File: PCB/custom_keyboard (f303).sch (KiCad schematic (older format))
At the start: 363 parts, among them J1 Conn_01x04, J2 SM04B-SRSS-TB(LF)(SN), SW1 SW_Push, SW2 SW_Push, U1 SRV05-4, U12 XC6206P332MR, U13 74LVC1G34, U14 STM32F303CBT6, X1 TestPoint_Small, X2 TestPoint_Small, Y2 8MHz

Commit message: Added indicator LED
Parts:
- added D1: Green, LED_SMD:LED_0805_2012Metric, symbol Device:LED_Small
- added R2: 680, Resistor_SMD:R_0805_2012Metric, symbol Device:R_Small
- R64: value 510 -> 680; LCSC Part C17734 -> C17798
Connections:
- net +3V3: now also J1.1 (Pin_1)
- net +5V: no longer D2.2 (A), F1.2, FB15.2, J2.1 (Pin_1), U1.5 (VP), USB1.11 (VBUS), USB1.2 (VBUS)
- net GND: now also R2.1
- net KEYBOARD_RESET: no longer J1.1 (Pin_1)
- net ROW3: now also D1.2 (A)
- new net: D1.1 (K), R2.2
- new net VBUS: D2.2 (A), F1.2, FB15.2, J2.1 (Pin_1), U1.5 (VP), USB1.11 (VBUS), USB1.2 (VBUS)
- no-connect marks 4 -> 6
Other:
- moved on the sheet: C1, D11, F1, J1, R64

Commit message: Removed encoder resistors and capacitors
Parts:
- removed C10, C11, C8, C9: 100nF, Capacitor_SMD:C_0805_2012Metric, symbol Device:C_Small
- removed R15, R16, R17, R18: 10k, Resistor_SMD:R_0805_2012Metric, symbol Device:R_Small
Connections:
- net ENCODER_A: now also ROT1.A, ROT2.A
- net ENCODER_B1: now also ROT1.B
- net ENCODER_B2: now also ROT2.B
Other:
- note added: "Keyboard Crystal"
- note removed: "Keyboard Crystals"
- moved on the sheet: BKL3, BOOT0, BOOT1, C18, C19, C20, C21, C22, C23, C24, C43, C44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

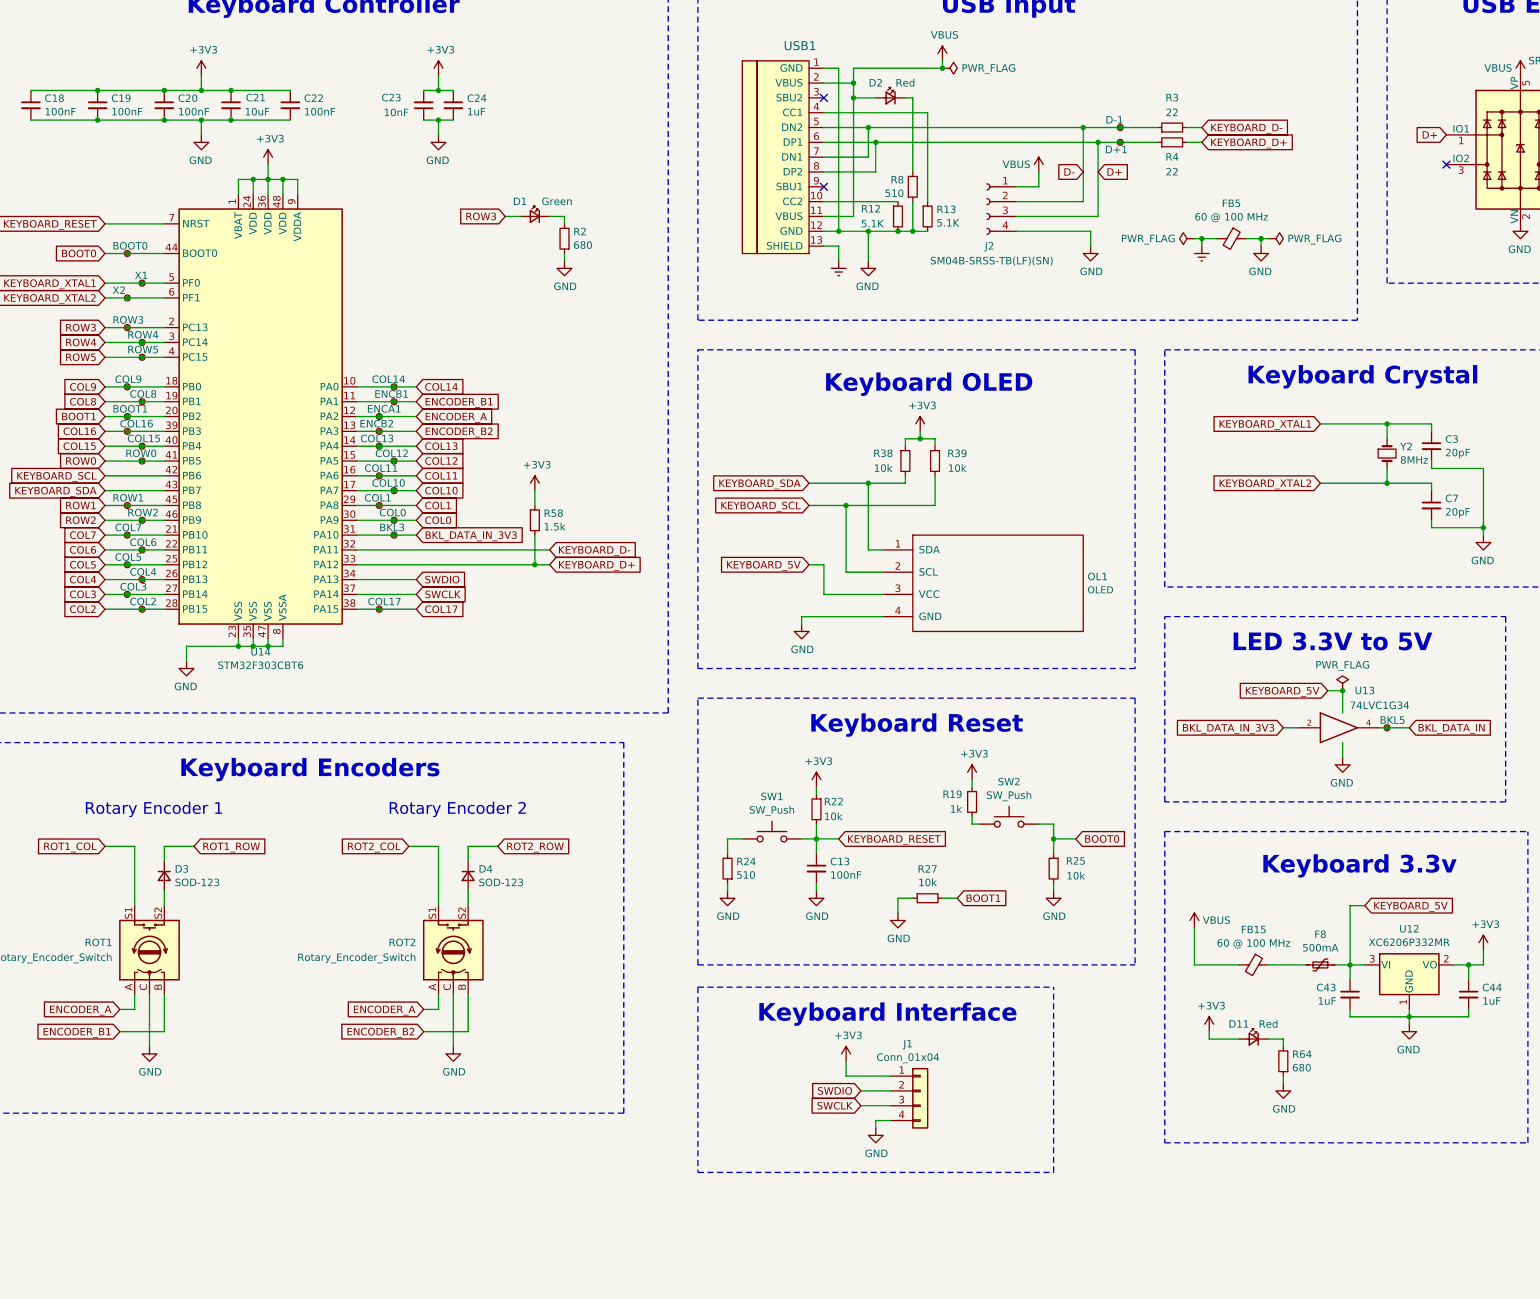
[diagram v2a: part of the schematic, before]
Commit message: Daisy chain routed diodes
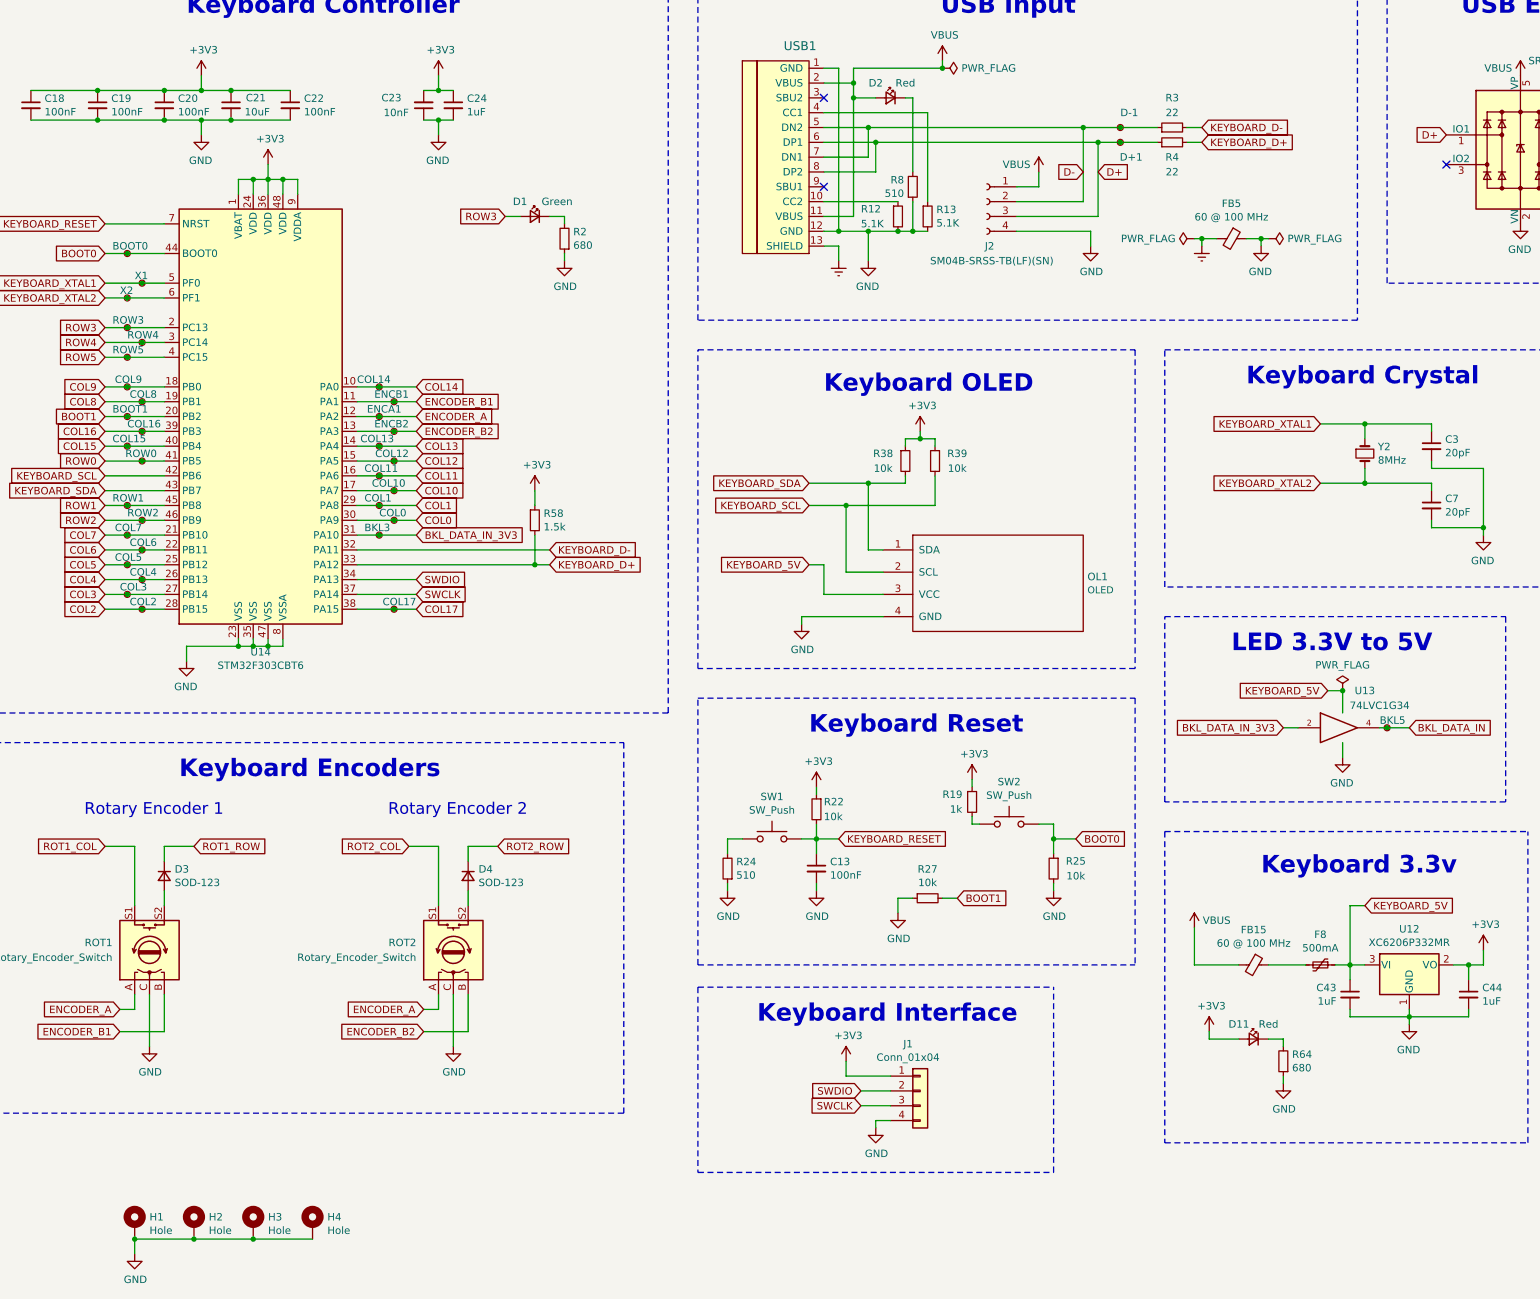
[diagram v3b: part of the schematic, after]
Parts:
- added H1, H2, H3, H4: Hole, MountingHole:MountingHole_3.2mm_M3_Pad, symbol Mechanical:MountingHole_Pad
- FB15, FB5: LCSC Part C237300 -> C337883
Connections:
- net GND: now also H1.1, H2.1, H3.1, H4.1
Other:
- moved on the sheet: BKL3, COL14, COL15, COL16, COL17, ENCB2, ROW5, Y2

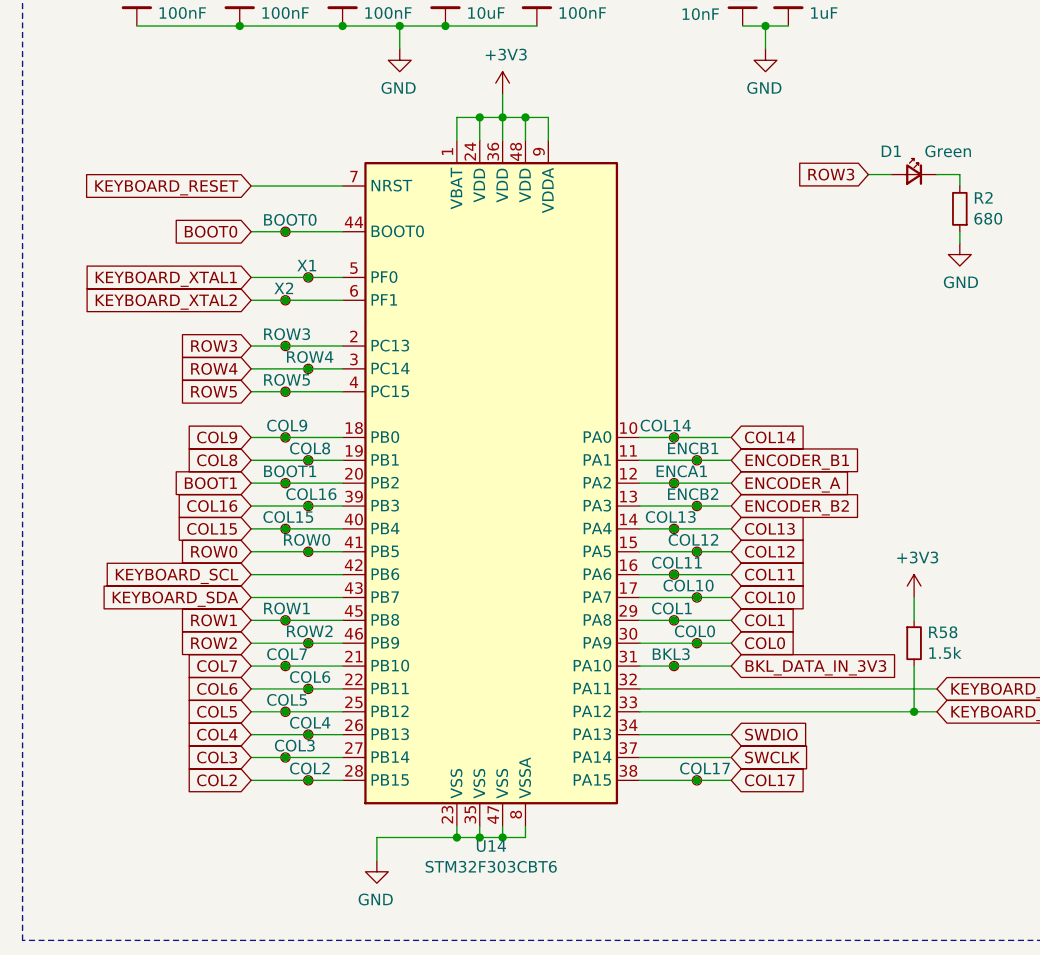
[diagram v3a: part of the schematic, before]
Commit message: Reassigned PC13/14/15
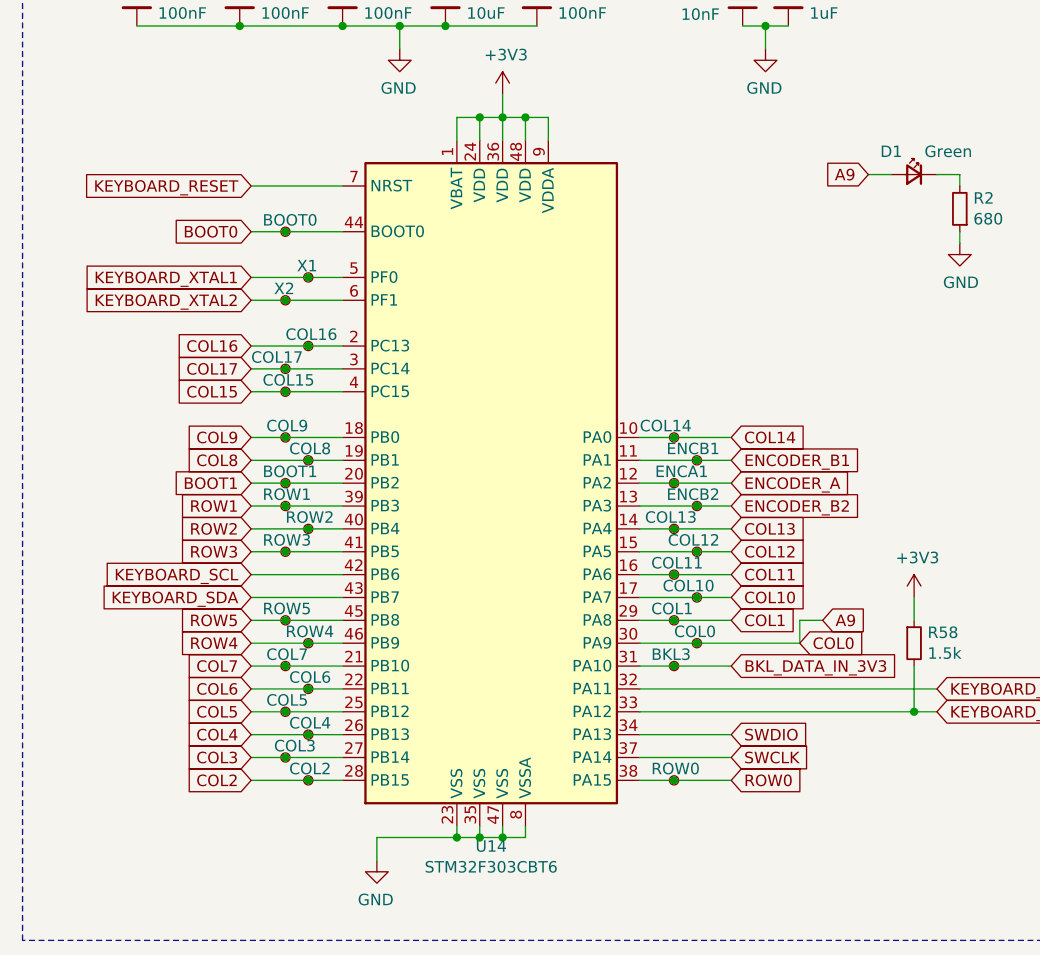
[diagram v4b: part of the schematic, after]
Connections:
- net COL15: now also U14.4 (PC15); no longer U14.40 (PB4)
- net COL16: now also U14.2 (PC13); no longer U14.39 (PB3)
- net COL17: now also U14.3 (PC14); no longer U14.38 (PA15)
- net ROT1_ROW: now also U14.38 (PA15); no longer U14.41 (PB5)
- net ROW1: now also U14.39 (PB3); no longer U14.45 (PB8)
- net ROW2: now also U14.40 (PB4); no longer U14.46 (PB9)
- net ROW3: now also U14.41 (PB5); no longer D1.2 (A), U14.2 (PC13)
- net ROW4: now also U14.46 (PB9); no longer U14.3 (PC14)
- net ROW5: now also U14.45 (PB8); no longer U14.4 (PC15)
- net COL0 renamed A9
- net A9: now also D1.2 (A)
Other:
- moved on the sheet: COL15, COL16, COL17, ROW0, ROW1, ROW2, ROW3, ROW4, ROW5

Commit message: Moved traces over by 1 gridline
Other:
- note added: "Mounting holes"
- moved on the sheet: D1, H1, H2, H3, H4, R2
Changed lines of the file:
@@
 Wire Notes Line
 	20050 11850 21850 11850
-Text Notes 17950 12150 2    118  ~ 24
+Text Notes 18100 12150 2    118  ~ 24
 USB Input
 Text GLabel 18000 13200 0    50   Input ~ 0
@@
 $EndComp
 Wire Wire Line
-	14500 13500 14500 13550
-Wire Wire Line
-	14400 13500 14500 13500
+	14300 13550 14300 13600
+Wire Wire Line
+	14200 13550 14300 13550
 $Comp
 L Device:R_Small R2
 U 1 1 75512E23
-P 14500 13650
-F 0 "R2" H 14441 13604 50  0000 R CNN
-F 1 "680" H 14441 13695 50  0000 R CNN
-F 2 "Resistor_SMD:R_0805_2012Metric" H 14500 13650 50  0001 C CNN
-F 3 "~" H 14500 13650 50  0001 C CNN
-F 4 "C17798" H 14500 13650 50  0001 C CNN "LCSC Part"
-	1    14500 13650
+P 14300 13700
+F 0 "R2" H 14241 13654 50  0000 R CNN
+F 1 "680" H 14241 13745 50  0000 R CNN
+F 2 "Resistor_SMD:R_0805_2012Metric" H 14300 13700 50  0001 C CNN
+F 3 "~" H 14300 13700 50  0001 C CNN
+F 4 "C17798" H 14300 13700 50  0001 C CNN "LCSC Part"
+	1    14300 13700
 	-1   0    0    1
 $EndComp
 Wire Wire Line
-	14500 13750 14500 13800
+	14300 13800 14300 13850
 $Comp
 L Device:LED_Small D1
 U 1 1 75512E2F
-P 14300 13500
-F 0 "D1" H 14400 13600 50  0000 C CNN
-F 1 "Green" H 14150 13600 50  0000 C CNN
-F 2 "LED_SMD:LED_0805_2012Metric" V 14300 13500 50  0001 C CNN
-F 3 "~" V 14300 13500 50  0001 C CNN
-F 4 "C84256" H 14300 13500 50  0001 C CNN "LCSC Part"
-	1    14300 13500
+P 14100 13550
+F 0 "D1" H 14200 13650 50  0000 C CNN
+F 1 "Green" H 13950 13650 50  0000 C CNN
+F 2 "LED_SMD:LED_0805_2012Metric" V 14100 13550 50  0001 C CNN
+F 3 "~" V 14100 13550 50  0001 C CNN
+F 4 "C84256" H 14100 13550 50  0001 C CNN "LCSC Part"
+	1    14100 13550
 	-1   0    0    -1
 $EndComp
@@
 L power:GND #PWR0194
 U 1 1 75512E39
-P 14500 13800
-F 0 "#PWR0194" H 14500 13550 50  0001 C CNN
-F 1 "GND" H 14505 13627 50  0000 C CNN
-F 2 "" H 14500 13800 50  0001 C CNN
-F 3 "" H 14500 13800 50  0001 C CNN
-	1    14500 13800
-	1    0    0    -1
-$EndComp
-Wire Wire Line
-	14200 13500 14100 13500
+P 14300 13850
+F 0 "#PWR0194" H 14300 13600 50  0001 C CNN
+F 1 "GND" H 14305 13677 50  0000 C CNN
+F 2 "" H 14300 13850 50  0001 C CNN
+F 3 "" H 14300 13850 50  0001 C CNN
+	1    14300 13850
+	1    0    0    -1
+$EndComp
+Wire Wire Line
+	14000 13550 13900 13550
 Text GLabel 13450 17750 0    50   Input ~ 0
 ROT2_COL
@@
 L Mechanical:MountingHole_Pad H1
 U 1 1 6C24E77E
-P 11600 20300
-F 0 "H1" H 11700 20349 50  0000 L CNN
-F 1 "Hole" H 11700 20258 50  0000 L CNN
-F 2 "MountingHole:MountingHole_3.2mm_M3_Pad" H 11600 20300 50  0001 C CNN
-F 3 "~" H 11600 20300 50  0001 C CNN
-	1    11600 20300
+P 21450 19250
+F 0 "H1" H 21550 19299 50  0000 L CNN
+F 1 "Hole" H 21550 19208 50  0000 L CNN
+F 2 "MountingHole:MountingHole_3.2mm_M3_Pad" H 21450 19250 50  0001 C CNN
+F 3 "~" H 21450 19250 50  0001 C CNN
+	1    21450 19250
 	1    0    0    -1
 $EndComp
@@
 L power:GND #PWR0199
 U 1 1 6C24F04A
-P 11600 20500
-F 0 "#PWR0199" H 11600 20250 50  0001 C CNN
-F 1 "GND" H 11605 20327 50  0000 C CNN
-F 2 "" H 11600 20500 50  0001 C CNN
-F 3 "" H 11600 20500 50  0001 C CNN
-	1    11600 20500
+P 21450 19450
+F 0 "#PWR0199" H 21450 19200 50  0001 C CNN
+F 1 "GND" H 21455 19277 50  0000 C CNN
+F 2 "" H 21450 19450 50  0001 C CNN
+F 3 "" H 21450 19450 50  0001 C CNN
+	1    21450 19450
 	1    0    0    -1
 $EndComp
@@
 L Mechanical:MountingHole_Pad H2
 U 1 1 6C24F523
-P 12000 20300
-F 0 "H2" H 12100 20349 50  0000 L CNN
-F 1 "Hole" H 12100 20258 50  0000 L CNN
-F 2 "MountingHole:MountingHole_3.2mm_M3_Pad" H 12000 20300 50  0001 C CNN
-F 3 "~" H 12000 20300 50  0001 C CNN
-	1    12000 20300
+P 21850 19250
+F 0 "H2" H 21950 19299 50  0000 L CNN
+F 1 "Hole" H 21950 19208 50  0000 L CNN
+F 2 "MountingHole:MountingHole_3.2mm_M3_Pad" H 21850 19250 50  0001 C CNN
+F 3 "~" H 21850 19250 50  0001 C CNN
+	1    21850 19250
 	1    0    0    -1
 $EndComp
@@
 L Mechanical:MountingHole_Pad H3
 U 1 1 6C24F72A
-P 12400 20300
-F 0 "H3" H 12500 20349 50  0000 L CNN
-F 1 "Hole" H 12500 20258 50  0000 L CNN
-F 2 "MountingHole:MountingHole_3.2mm_M3_Pad" H 12400 20300 50  0001 C CNN
-F 3 "~" H 12400 20300 50  0001 C CNN
-	1    12400 20300
+P 22250 19250
+F 0 "H3" H 22350 19299 50  0000 L CNN
+F 1 "Hole" H 22350 19208 50  0000 L CNN
+F 2 "MountingHole:MountingHole_3.2mm_M3_Pad" H 22250 19250 50  0001 C CNN
+F 3 "~" H 22250 19250 50  0001 C CNN
+	1    22250 19250
 	1    0    0    -1
 $EndComp
@@
 L Mechanical:MountingHole_Pad H4
 U 1 1 6C24FA2A
-P 12800 20300
-F 0 "H4" H 12900 20349 50  0000 L CNN
-F 1 "Hole" H 12900 20258 50  0000 L CNN
-F 2 "MountingHole:MountingHole_3.2mm_M3_Pad" H 12800 20300 50  0001 C CNN
-F 3 "~" H 12800 20300 50  0001 C CNN
-	1    12800 20300
-	1    0    0    -1
-$EndComp
-Wire Wire Line
-	12800 20400 12400 20400
-Connection ~ 12000 20400
-Wire Wire Line
-	12000 20400 11600 20400
-Connection ~ 12400 20400
-Wire Wire Line
-	12400 20400 12000 20400
-Wire Wire Line
-	11600 20500 11600 20400
-Connection ~ 11600 20400
+P 22650 19250
+F 0 "H4" H 22750 19299 50  0000 L CNN
+F 1 "Hole" H 22750 19208 50  0000 L CNN
+F 2 "MountingHole:MountingHole_3.2mm_M3_Pad" H 22650 19250 50  0001 C CNN
+F 3 "~" H 22650 19250 50  0001 C CNN
+	1    22650 19250
+	1    0    0    -1
+$EndComp
+Wire Wire Line
+	22650 19350 22250 19350
+Connection ~ 21850 19350
+Wire Wire Line
+	21850 19350 21450 19350
+Connection ~ 22250 19350
+Wire Wire Line
+	22250 19350 21850 19350
+Wire Wire Line
+	21450 19450 21450 19350
+Connection ~ 21450 19350
 Text GLabel 13900 15450 2    50   Input ~ 0
 A9
@@
 Wire Wire Line
 	13800 15450 13800 15550
-Text GLabel 14100 13500 0    50   Input ~ 0
+Text GLabel 13900 13550 0    50   Input ~ 0
 A9
 Wire Notes Line
@@
 Text GLabel 11400 15450 0    50   Input ~ 0
 ROW5
+Text Notes 21450 19000 0    118  ~ 24
+Mounting holes
+Wire Notes Line
+	21200 18750 23050 18750
+Wire Notes Line
+	23050 18750 23050 19750
+Wire Notes Line
+	23050 19750 21200 19750
+Wire Notes Line
+	21200 19750 21200 18750
 $EndSCHEMATC
